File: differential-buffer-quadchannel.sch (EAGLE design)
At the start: 55 parts, among them U1 AD8421, U2 AD8421, U3 AD8421, U4 AD8421

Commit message: Added part numbers
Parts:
- C17, C18: value (none) -> 220uF; PARTNO (none) -> PCE3955CT-ND
- JP1: PARTNO (none) -> WM4201-ND
- OUT_CH0, OUT_CH1, OUT_CH2, OUT_CH3: PARTNO (none) -> A32260-ND
- R1, R11, R12, R3, R5, R6, R8, R9: PARTNO (none) -> P49.9HCT-ND
- R10, R2, R4, R7: value 10k -> 1M; PARTNO TNP10.0KAACT-ND -> P1.00MHCT-ND
- RG0, RG1, RG2, RG3: value (none) -> DNP
- U1, U2, U3, U4: PARTNO (none) -> AD8421ARZ-R7CT-ND

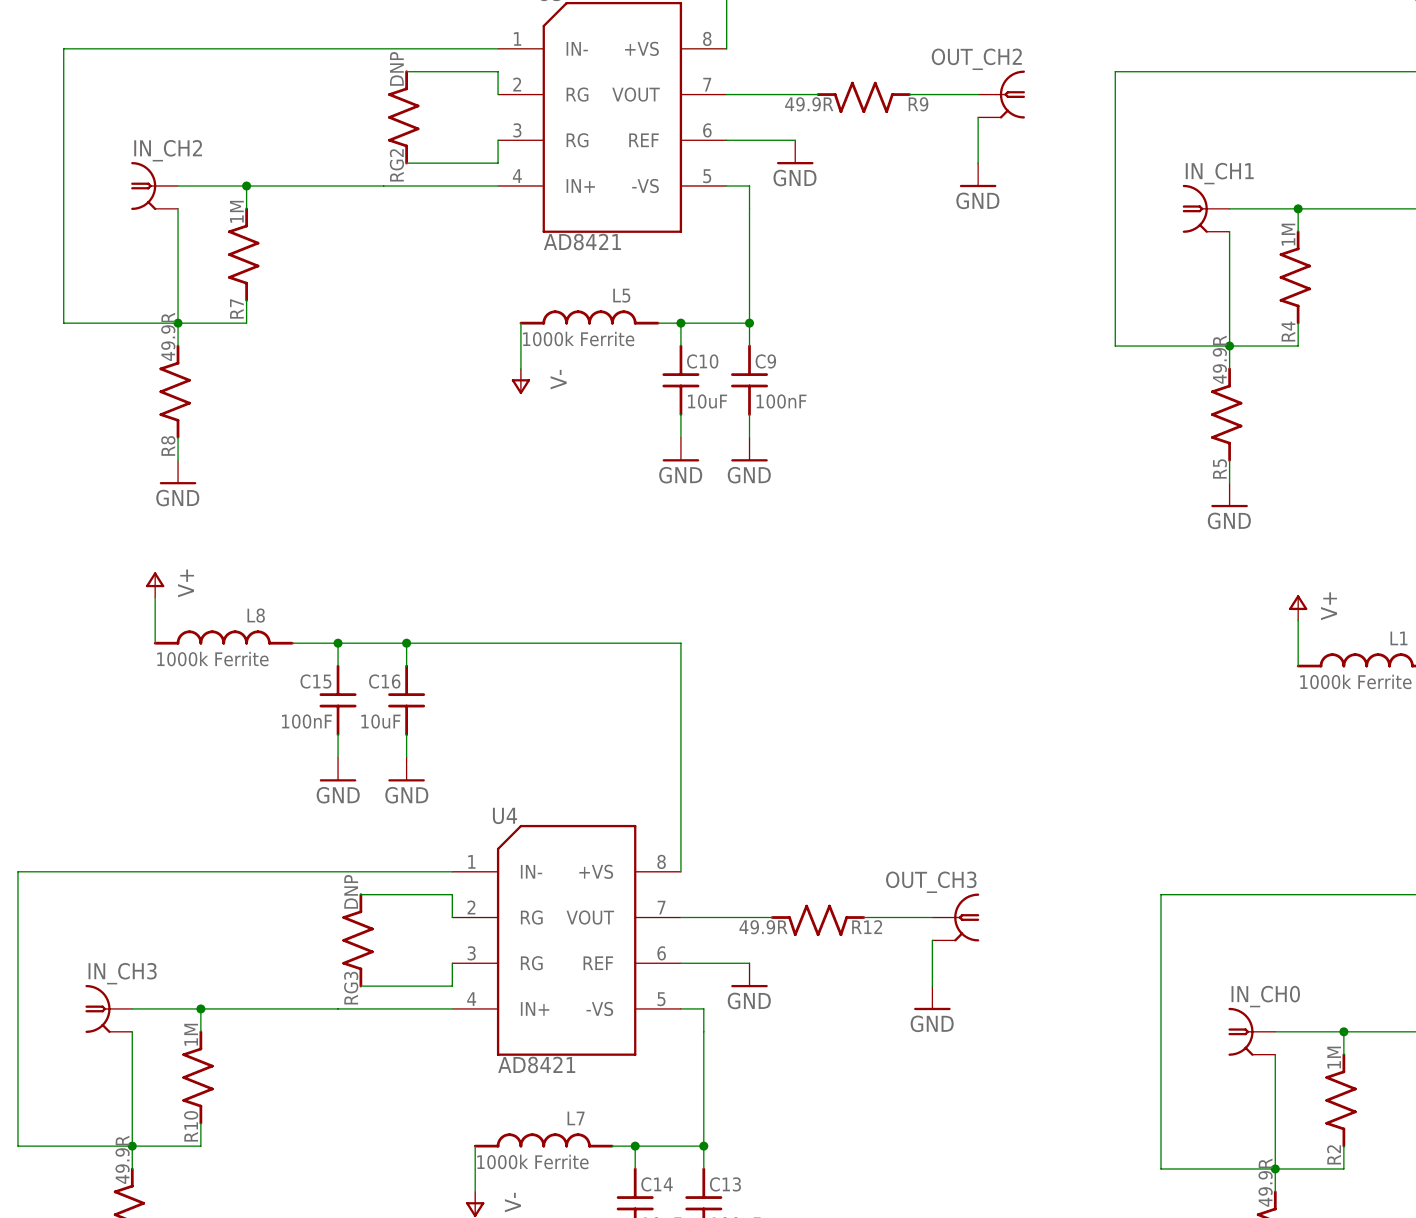
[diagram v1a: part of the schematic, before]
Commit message: changed RA BNC to vertical
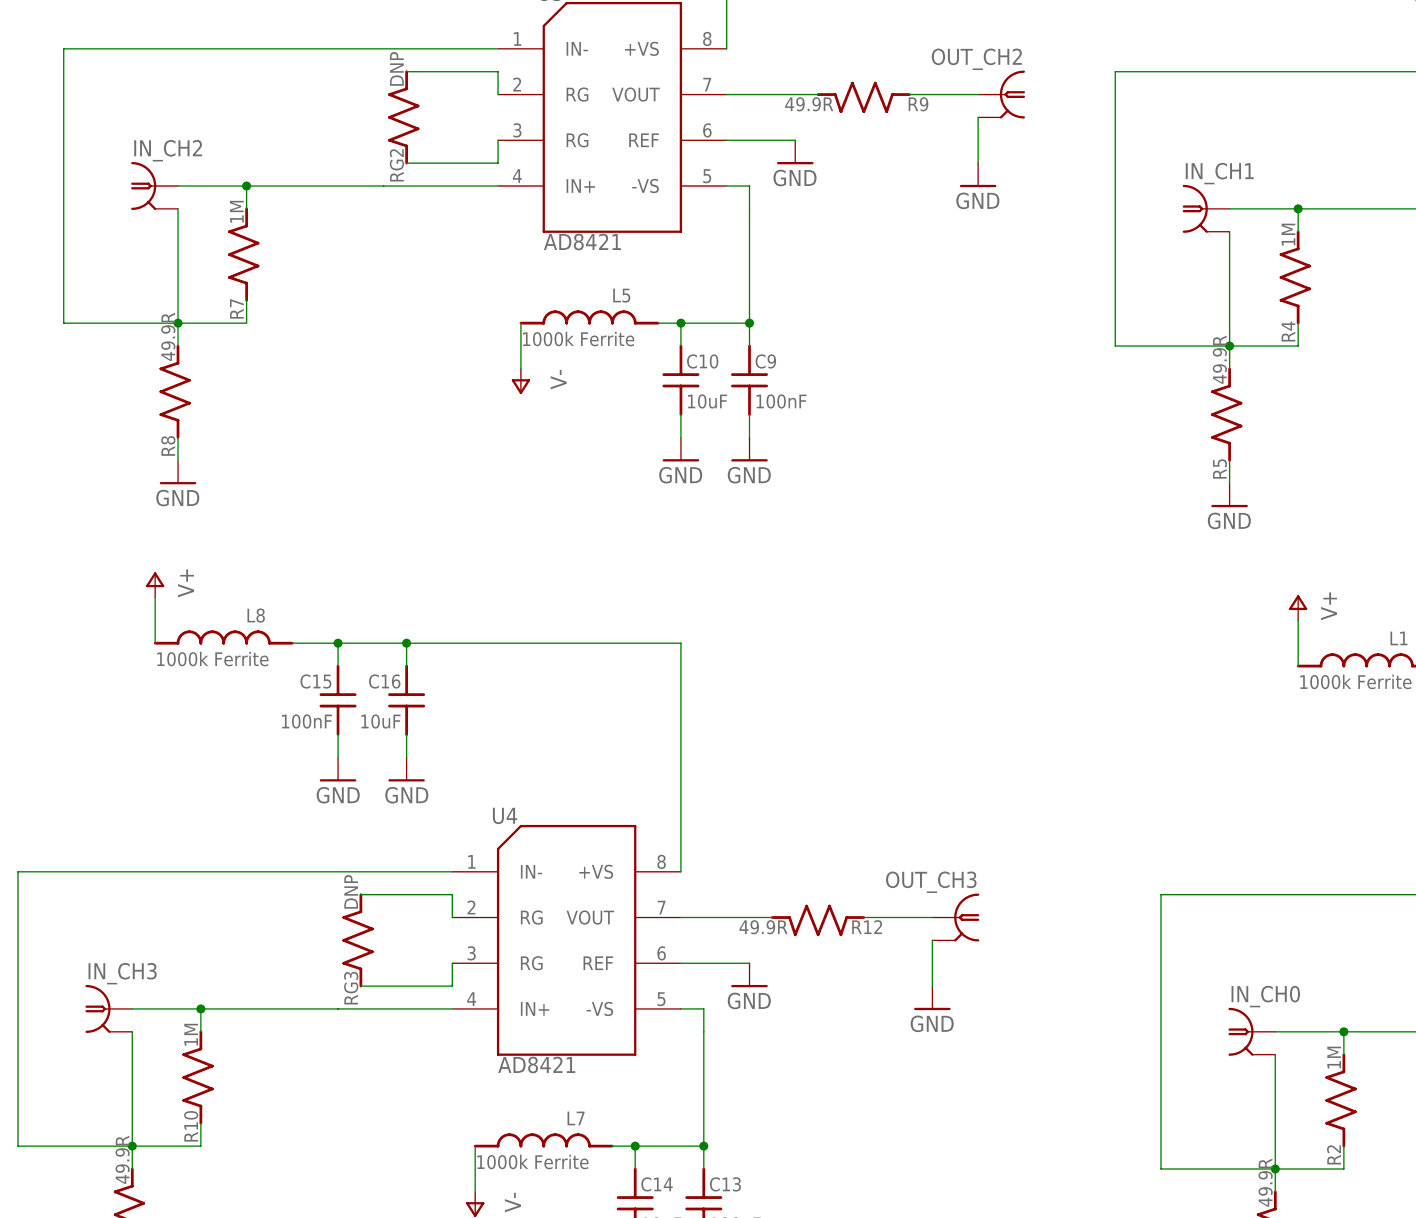
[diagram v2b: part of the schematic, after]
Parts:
- IN_CH0, IN_CH1, IN_CH2, IN_CH3: value BNC-H -> BNC-V; device Eurocard-HV-piezo-driver:BNC-H -> connector-jqi:BNC-V; PARTNO A32260-ND -> (none)
- OUT_CH0, OUT_CH1, OUT_CH2, OUT_CH3: value BNC-H -> BNC-V; device connector-jqi:BNC-H -> connector-jqi:BNC-V; PARTNO A32260-ND -> (none)
